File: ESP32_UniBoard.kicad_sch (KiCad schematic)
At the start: 21 parts, among them J1 USB_C_Receptacle_USB2.0, J2 Conn_01x06_Socket, J3 Hirose DF40C, SW1 SW_Push, SW2 SW_Push, U1 ESP32-S3-WROOM-1, U2 SPX3819M5-L-3-3

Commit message: Schematics and PCB updates
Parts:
- added C9: 100nF, Capacitor_SMD:C_0603_1608Metric_Pad1.08x0.95mm_HandSolder, symbol Device:C_Small
- added D3: RED, LED_SMD:LED_0603_1608Metric_Pad1.05x0.95mm_HandSolder, symbol Device:LED
- added D4: YL, LED_SMD:LED_0603_1608Metric_Pad1.05x0.95mm_HandSolder, symbol Device:LED
- added F1: Polyfuse, Fuse:Fuse_1206_3216Metric_Pad1.42x1.75mm_HandSolder, symbol Device:Polyfuse
- added R5, R6: R, Resistor_SMD:R_0603_1608Metric_Pad0.98x0.95mm_HandSolder, symbol Device:R
- added U3: USBLC6-2SC6, Package_TO_SOT_SMD:SOT-23-6, symbol Power_Protection:USBLC6-2SC6
- D2: renamed from D1; value LED -> GRN
- renumbered D2 to D1
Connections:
- net BOOT: now also J3.31 (Pin_31); no longer J3.34 (Pin_34)
- net ESP_RX: now also J3.17 (Pin_17), R5.1; no longer J3.45 (Pin_45)
- net ESP_TX: now also J3.16 (Pin_16); no longer J3.46 (Pin_46)
- net GND: now also C9.2, D3.1 (K), D4.1 (K), U3.2 (GND)
- net GPIO1: now also J3.14 (Pin_14); no longer J3.48 (Pin_48)
- net GPIO10: now also J3.42 (Pin_42); no longer J3.20 (Pin_20)
- net GPIO11: now also J3.41 (Pin_41); no longer J3.21 (Pin_21)
- net GPIO12: now also J3.40 (Pin_40); no longer J3.22 (Pin_22)
- net GPIO13: now also J3.39 (Pin_39); no longer J3.23 (Pin_23)
- net GPIO14: now also J3.37 (Pin_37); no longer J3.28 (Pin_28)
- net GPIO16: now also J3.6 (Pin_6); no longer J3.9 (Pin_9)
- net GPIO17: now also J3.5 (Pin_5); no longer J3.10 (Pin_10)
- net GPIO18: now also J3.4 (Pin_4); no longer J3.11 (Pin_11)
- net GPIO2: now also J3.15 (Pin_15); no longer J3.47 (Pin_47)
- net GPIO21: now also J3.36 (Pin_36); no longer J3.29 (Pin_29)
- net GPIO3: now also J3.46 (Pin_46); no longer J3.16 (Pin_16)
- net GPIO35: now also J3.30 (Pin_30), R6.1; no longer J3.35 (Pin_35)
- net GPIO36: now also J3.29 (Pin_29); no longer J3.36 (Pin_36)
- net GPIO37: now also J3.28 (Pin_28); no longer J3.37 (Pin_37)
- net GPIO38: now also J3.23 (Pin_23); no longer J3.39 (Pin_39)
- net GPIO39: now also J3.22 (Pin_22); no longer J3.40 (Pin_40)
- net GPIO4: now also J3.12 (Pin_12); no longer J3.3 (Pin_3)
- net GPIO40: now also J3.21 (Pin_21); no longer J3.41 (Pin_41)
- net GPIO41: now also J3.20 (Pin_20); no longer J3.42 (Pin_42)
- net GPIO42: now also J3.19 (Pin_19); no longer J3.44 (Pin_44)
- net GPIO46: now also J3.45 (Pin_45); no longer J3.17 (Pin_17)
- net GPIO47: now also J3.35 (Pin_35); no longer J3.30 (Pin_30)
- net GPIO48: now also J3.34 (Pin_34); no longer J3.31 (Pin_31)
- net GPIO5: now also J3.11 (Pin_11); no longer J3.4 (Pin_4)
- net GPIO6: now also J3.10 (Pin_10); no longer J3.5 (Pin_5)
- net GPIO7: now also J3.9 (Pin_9); no longer J3.6 (Pin_6)
- net GPIO8: now also J3.3 (Pin_3); no longer J3.12 (Pin_12)
- net GPIO9: now also J3.44 (Pin_44); no longer J3.19 (Pin_19)
- net USB_D_N: now also J3.47 (Pin_47), U3.1 (I/O1), U3.6 (I/O1); no longer J3.14 (Pin_14)
- net USB_D_P: now also J3.48 (Pin_48), U3.3 (I/O2), U3.4 (I/O2); no longer J3.15 (Pin_15)
- net VBUS: now reaches J1.A4 (VBUS), J1.A9 (VBUS), J1.B4 (VBUS), J1.B9 (VBUS)
- net VBUS: now also C9.1, F1.1, U3.5 (VBUS); no longer D1.2 (A)
- new net: D1.2 (A), F1.2
- new net: D3.2 (A), R5.2
- new net: D4.2 (A), R6.2
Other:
- note added: "GPIO1"
- note added: "PWR"
- note added: "RX"
- moved on the sheet: C2, C5, C6, C7, C8, D1, D2, R4, SW1, SW2, U2

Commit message: Start of PCB routing
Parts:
- added H1, H2, H3, H4: MountingHole, MountingHole:MountingHole_2.7mm_M2.5, symbol Mechanical:MountingHole
- F1: footprint Fuse:Fuse_1206_3216Metric_Pad1.42x1.75mm_HandSolder -> Fuse:Fuse_0805_2012Metric_Pad1.15x1.40mm_HandSolder
- SW1, SW2: footprint Button_Switch_SMD:SW_SPST_PTS645 -> Button_Switch_SMD:SW_Tactile_SPST_NO_Straight_CK_PTS636Sx25SMTRLFS
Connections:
- net GPIO3: now also J3.45 (Pin_45); no longer J3.46 (Pin_46)
- net GPIO46: now also J3.46 (Pin_46); no longer J3.45 (Pin_45)
- net USB_D_N renamed DPr_N
- net DPr_N: no longer J1.A7 (D-), J1.B7 (D-), U3.1 (I/O1)
- net USB_D_P renamed DPr_P
- net DPr_P: no longer J1.A6 (D+), J1.B6 (D+), U3.3 (I/O2)
- new net D_N: J1.A7 (D-), J1.B7 (D-), U3.1 (I/O1)
- new net D_P: J1.A6 (D+), J1.B6 (D+), U3.3 (I/O2)
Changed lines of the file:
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@@
   (no_connect (at 22.86 88.9))
   (no_connect (at 45.72 58.42))
-  (no_connect (at 45.974 81.026))
+  (no_connect (at 45.72 81.28))
   (no_connect (at 45.72 55.88))
   (no_connect (at 45.72 71.12))
-  (no_connect (at 45.974 78.486))
+  (no_connect (at 45.72 78.74))
   (no_connect (at 45.72 66.04))
   (no_connect (at 45.72 48.26))
@@
     (effects (font (size 1.27 1.27)) (justify right bottom))
   )
-  (label "USB_D_N" (at 86.995 132.08 180) (fields_autoplaced)
+  (label "DPr_N" (at 86.995 132.08 180) (fields_autoplaced)
     (effects (font (size 1.27 1.27)) (justify right bottom))
   )
@@
     (effects (font (size 1.27 1.27)) (justify right bottom))
   )
-  (label "USB_D_P" (at 101.6 53.34 180) (fields_autoplaced)
+  (label "DPr_P" (at 101.6 53.34 180) (fields_autoplaced)
     (effects (font (size 1.27 1.27)) (justify right bottom))
   )
@@
     (effects (font (size 1.27 1.27)) (justify left bottom))
   )
-  (label "USB_D_N" (at 62.23 53.34 0) (fields_autoplaced)
+  (label "DPr_N" (at 62.23 53.34 0) (fields_autoplaced)
     (effects (font (size 1.27 1.27)) (justify left bottom))
   )
@@
     (effects (font (size 1.27 1.27)) (justify right bottom))
   )
-  (label "GPIO46" (at 86.995 137.16 180) (fields_autoplaced)
+  (label "GPIO46" (at 86.995 134.62 180) (fields_autoplaced)
     (effects (font (size 1.27 1.27)) (justify right bottom))
   )
@@
     (effects (font (size 1.27 1.27)) (justify right bottom))
   )
-  (label "USB_D_P" (at 86.995 129.54 180) (fields_autoplaced)
+  (label "DPr_P" (at 86.995 129.54 180) (fields_autoplaced)
     (effects (font (size 1.27 1.27)) (justify right bottom))
   )
@@
     (effects (font (size 1.27 1.27)) (justify right bottom))
   )
-  (label "USB_D_N" (at 62.23 58.42 0) (fields_autoplaced)
+  (label "D_N" (at 62.23 58.42 0) (fields_autoplaced)
     (effects (font (size 1.27 1.27)) (justify left bottom))
   )
@@
     (effects (font (size 1.27 1.27)) (justify right bottom))
   )
-  (label "USB_D_N" (at 278.13 41.91 180) (fields_autoplaced)
+  (label "DPr_N" (at 278.13 41.91 180) (fields_autoplaced)
     (effects (font (size 1.27 1.27)) (justify right bottom))
   )
@@
     (effects (font (size 1.27 1.27)) (justify right bottom))
   )
-  (label "USB_D_N" (at 56.642 35.56 180) (fields_autoplaced)
+  (label "D_N" (at 56.642 35.56 180) (fields_autoplaced)
     (effects (font (size 1.27 1.27)) (justify right bottom))
   )
@@
     (effects (font (size 1.27 1.27)) (justify left bottom))
   )
-  (label "GPIO3" (at 86.995 134.62 180) (fields_autoplaced)
+  (label "GPIO3" (at 86.995 137.16 180) (fields_autoplaced)
     (effects (font (size 1.27 1.27)) (justify right bottom))
   )
@@
     (effects (font (size 1.27 1.27)) (justify right bottom))
   )
-  (label "USB_D_P" (at 56.642 40.64 180) (fields_autoplaced)
+  (label "D_P" (at 56.642 40.64 180) (fields_autoplaced)
     (effects (font (size 1.27 1.27)) (justify right bottom))
   )
@@
     (effects (font (size 1.27 1.27)) (justify left bottom))
   )
-  (label "USB_D_P" (at 278.13 39.37 180) (fields_autoplaced)
+  (label "DPr_P" (at 278.13 39.37 180) (fields_autoplaced)
     (effects (font (size 1.27 1.27)) (justify right bottom))
   )
@@
     (effects (font (size 1.27 1.27)) (justify right bottom))
   )
-  (label "USB_D_P" (at 101.6 58.42 180) (fields_autoplaced)
+  (label "D_P" (at 101.6 58.42 180) (fields_autoplaced)
     (effects (font (size 1.27 1.27)) (justify right bottom))
   )
@@
       (effects (font (size 1.27 1.27)) hide)
     )
-    (property "Footprint" "Button_Switch_SMD:SW_SPST_PTS645" (at 260.35 129.54 0)
+    (property "Footprint" "Button_Switch_SMD:SW_Tactile_SPST_NO_Straight_CK_PTS636Sx25SMTRLFS" (at 260.35 129.54 0)
       (effects (font (size 1.27 1.27)) hide)
     )
@@
       (effects (font (size 1.27 1.27)) hide)
     )
-    (property "Footprint" "Button_Switch_SMD:SW_SPST_PTS645" (at 260.35 112.395 0)
+    (property "Footprint" "Button_Switch_SMD:SW_Tactile_SPST_NO_Straight_CK_PTS636Sx25SMTRLFS" (at 260.35 112.395 0)
       (effects (font (size 1.27 1.27)) hide)
     )
@@
         (path "/5887f50f-f688-4449-b0b1-5b01ba454700"
           (reference "#PWR035") (unit 1)
+        )
+      )
+    )
+  )
+  (symbol (lib_id "Mechanical:MountingHole") (at 21.59 178.308 0) (unit 1)
+    (in_bom yes) (on_board yes) (dnp no) (fields_autoplaced)
+    (property "Reference" "H3" (at 24.892 177.673 0)
+      (effects (font (size 1.27 1.27)) (justify left))
+    )
+    (property "Value" "MountingHole" (at 24.892 180.213 0)
+      (effects (font (size 1.27 1.27)) (justify left))
+    )
+    (property "Footprint" "MountingHole:MountingHole_2.7mm_M2.5" (at 21.59 178.308 0)
+      (effects (font (size 1.27 1.27)) hide)
+    )
+    (property "Datasheet" "~" (at 21.59 178.308 0)
+      (effects (font (size 1.27 1.27)) hide)
+    )
+    (instances
+      (project "ESP32_UniBoard"
+        (path "/5887f50f-f688-4449-b0b1-5b01ba454700"
+          (reference "H3") (unit 1)
         )
       )
@@
       (effects (font (size 1.27 1.27)) hide)
     )
-    (property "Footprint" "Fuse:Fuse_1206_3216Metric_Pad1.42x1.75mm_HandSolder" (at 58.42 21.59 0)
+    (property "Footprint" "Fuse:Fuse_0805_2012Metric_Pad1.15x1.40mm_HandSolder" (at 58.42 21.59 0)
       (effects (font (size 1.27 1.27)) (justify left) hide)
     )
@@
         (path "/5887f50f-f688-4449-b0b1-5b01ba454700"
           (reference "#PWR026") (unit 1)
+        )
+      )
+    )
+  )
+  (symbol (lib_id "Mechanical:MountingHole") (at 22.352 191.262 0) (unit 1)
+    (in_bom yes) (on_board yes) (dnp no) (fields_autoplaced)
+    (property "Reference" "H1" (at 25.4 190.627 0)
+      (effects (font (size 1.27 1.27)) (justify left))
+    )
+    (property "Value" "MountingHole" (at 25.4 193.167 0)
+      (effects (font (size 1.27 1.27)) (justify left))
+    )
+    (property "Footprint" "MountingHole:MountingHole_2.7mm_M2.5" (at 22.352 191.262 0)
+      (effects (font (size 1.27 1.27)) hide)
+    )
+    (property "Datasheet" "~" (at 22.352 191.262 0)
+      (effects (font (size 1.27 1.27)) hide)
+    )
+    (instances
+      (project "ESP32_UniBoard"
+        (path "/5887f50f-f688-4449-b0b1-5b01ba454700"
+          (reference "H1") (unit 1)
         )
       )
@@
     )
   )
+  (symbol (lib_id "Mechanical:MountingHole") (at 21.844 170.942 0) (unit 1)
+    (in_bom yes) (on_board yes) (dnp no) (fields_autoplaced)
+    (property "Reference" "H4" (at 25.146 170.307 0)
+      (effects (font (size 1.27 1.27)) (justify left))
+    )
+    (property "Value" "MountingHole" (at 25.146 172.847 0)
+      (effects (font (size 1.27 1.27)) (justify left))
+    )
+    (property "Footprint" "MountingHole:MountingHole_2.7mm_M2.5" (at 21.844 170.942 0)
+      (effects (font (size 1.27 1.27)) hide)
+    )
+    (property "Datasheet" "~" (at 21.844 170.942 0)
+      (effects (font (size 1.27 1.27)) hide)
+    )
+    (instances
+      (project "ESP32_UniBoard"
+        (path "/5887f50f-f688-4449-b0b1-5b01ba454700"
+          (reference "H4") (unit 1)
+        )
+      )
+    )
+  )
   (symbol (lib_id "Device:C_Small") (at 145.415 26.67 0) (unit 1)
     (in_bom yes) (on_board yes) (dnp no)
@@
         )
       )
+    )
+  )
+  (symbol (lib_id "Mechanical:MountingHole") (at 22.098 184.658 0) (unit 1)
+    (in_bom yes) (on_board yes) (dnp no) (fields_autoplaced)
+    (property "Reference" "H2" (at 25.4 184.023 0)
+      (effects (font (size 1.27 1.27)) (justify left))
+    )
+    (property "Value" "MountingHole" (at 25.4 186.563 0)
+      (effects (font (size 1.27 1.27)) (justify left))
+    )
+    (property "Footprint" "MountingHole:MountingHole_2.7mm_M2.5" (at 22.098 184.658 0)
+      (effects (font (size 1.27 1.27)) hide)
+    )
+    (property "Datasheet" "~" (at 22.098 184.658 0)
+      (effects (font (size 1.27 1.27)) hide)
+    )
+    (instances
+      (project "ESP32_UniBoard"
+        (path "/5887f50f-f688-4449-b0b1-5b01ba454700"
+          (reference "H2") (unit 1)
+        )
+      )

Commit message: Routing complete
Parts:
- removed H4: MountingHole, MountingHole:MountingHole_2.7mm_M2.5, symbol Mechanical:MountingHole
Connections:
- net BOOT: now also J3.21 (Pin_21); no longer J3.31 (Pin_31)
- net DPr_N: now also J3.5 (Pin_5); no longer J3.47 (Pin_47)
- net DPr_P: now also J3.4 (Pin_4); no longer J3.48 (Pin_48)
- net ESP_RX: now also J3.35 (Pin_35); no longer J3.17 (Pin_17)
- net ESP_TX: now also J3.36 (Pin_36); no longer J3.16 (Pin_16)
- net GPIO1: now also J3.39 (Pin_39), R6.1; no longer J3.14 (Pin_14)
- net GPIO10: now also J3.10 (Pin_10); no longer J3.42 (Pin_42)
- net GPIO11: now also J3.11 (Pin_11); no longer J3.41 (Pin_41)
- net GPIO12: now also J3.12 (Pin_12); no longer J3.40 (Pin_40)
- net GPIO13: now also J3.14 (Pin_14); no longer J3.39 (Pin_39)
- net GPIO14: now also J3.15 (Pin_15); no longer J3.37 (Pin_37)
- net GPIO15: now also J3.45 (Pin_45); no longer J3.7 (Pin_7)
- net GPIO16: now also J3.46 (Pin_46); no longer J3.6 (Pin_6)
- net GPIO17: now also J3.47 (Pin_47); no longer J3.5 (Pin_5)
- net GPIO18: now also J3.48 (Pin_48); no longer J3.4 (Pin_4)
- net GPIO2: now also J3.37 (Pin_37); no longer J3.15 (Pin_15)
- net GPIO21: now also J3.16 (Pin_16); no longer J3.36 (Pin_36)
- net GPIO3: now also J3.6 (Pin_6); no longer J3.45 (Pin_45)
- net GPIO35: now also J3.22 (Pin_22); no longer J3.30 (Pin_30), R6.1
- net GPIO36: now also J3.23 (Pin_23); no longer J3.29 (Pin_29)
- net GPIO38: now also J3.29 (Pin_29); no longer J3.23 (Pin_23)
- net GPIO39: now also J3.30 (Pin_30); no longer J3.22 (Pin_22)
- net GPIO4: now also J3.40 (Pin_40); no longer J3.12 (Pin_12)
- net GPIO40: now also J3.31 (Pin_31); no longer J3.21 (Pin_21)
- net GPIO41: now also J3.32 (Pin_32); no longer J3.20 (Pin_20)
- net GPIO42: now also J3.34 (Pin_34); no longer J3.19 (Pin_19)
- net GPIO45: now also J3.20 (Pin_20); no longer J3.32 (Pin_32)
- net GPIO46: now also J3.7 (Pin_7); no longer J3.46 (Pin_46)
- net GPIO47: now also J3.17 (Pin_17); no longer J3.35 (Pin_35)
- net GPIO48: now also J3.19 (Pin_19); no longer J3.34 (Pin_34)
- net GPIO5: now also J3.41 (Pin_41); no longer J3.11 (Pin_11)
- net GPIO6: now also J3.42 (Pin_42); no longer J3.10 (Pin_10)
- net GPIO7: now also J3.44 (Pin_44); no longer J3.9 (Pin_9)
- net GPIO9: now also J3.9 (Pin_9); no longer J3.44 (Pin_44)

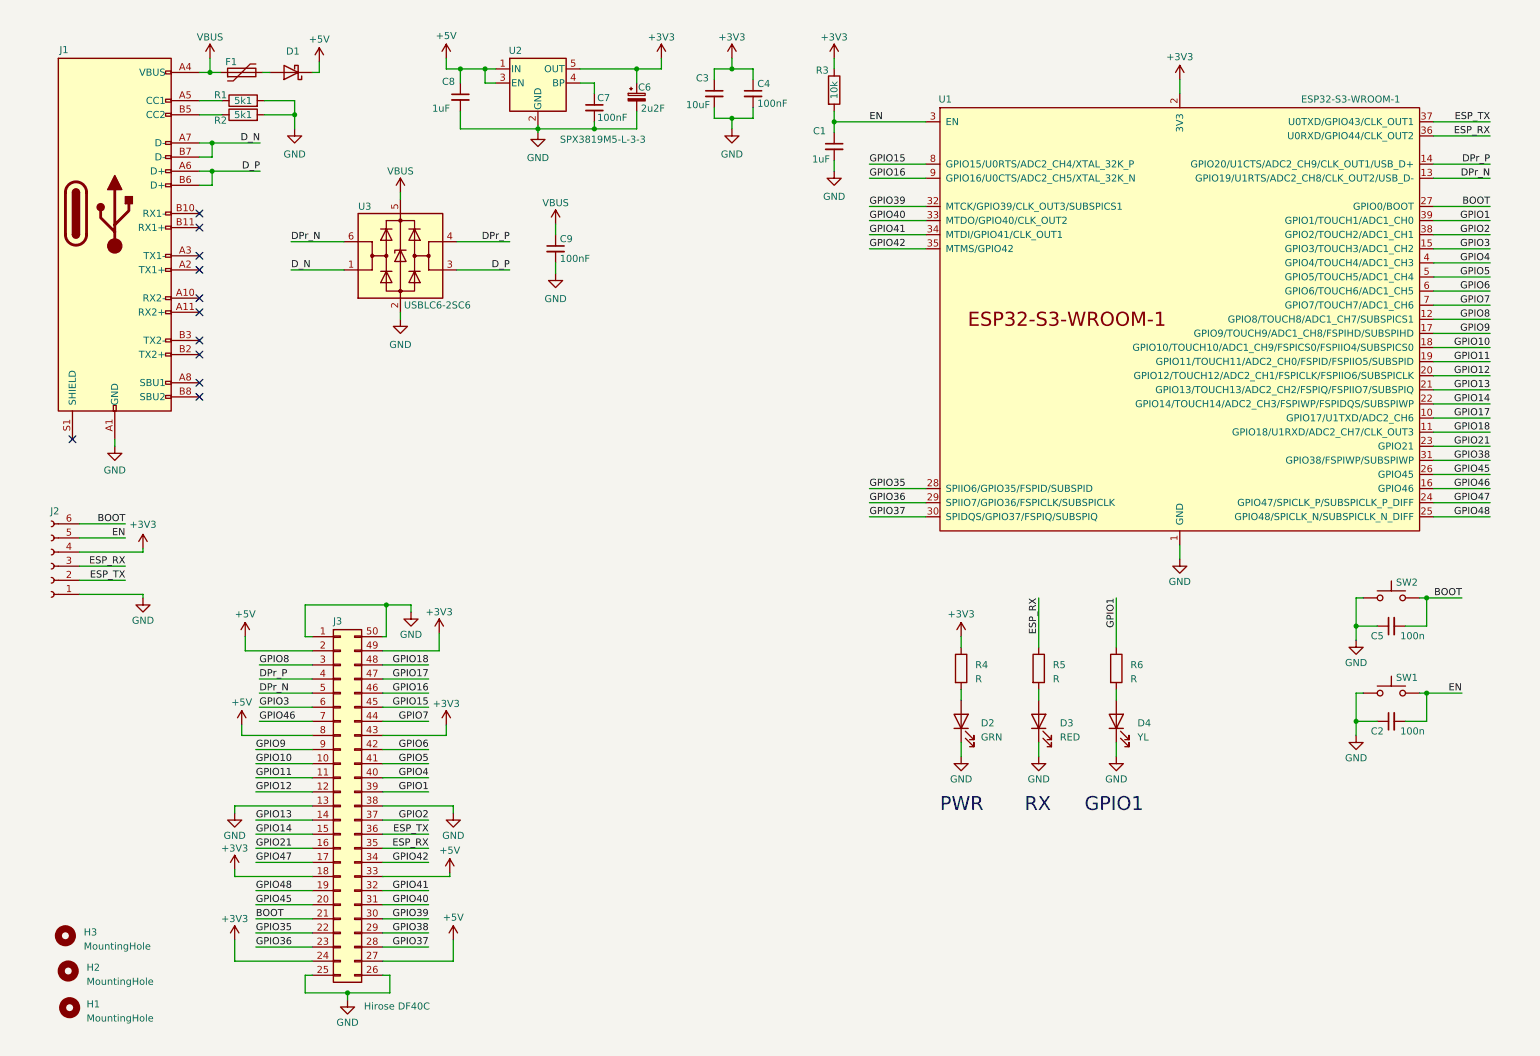
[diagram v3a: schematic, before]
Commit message: Screenshots generated
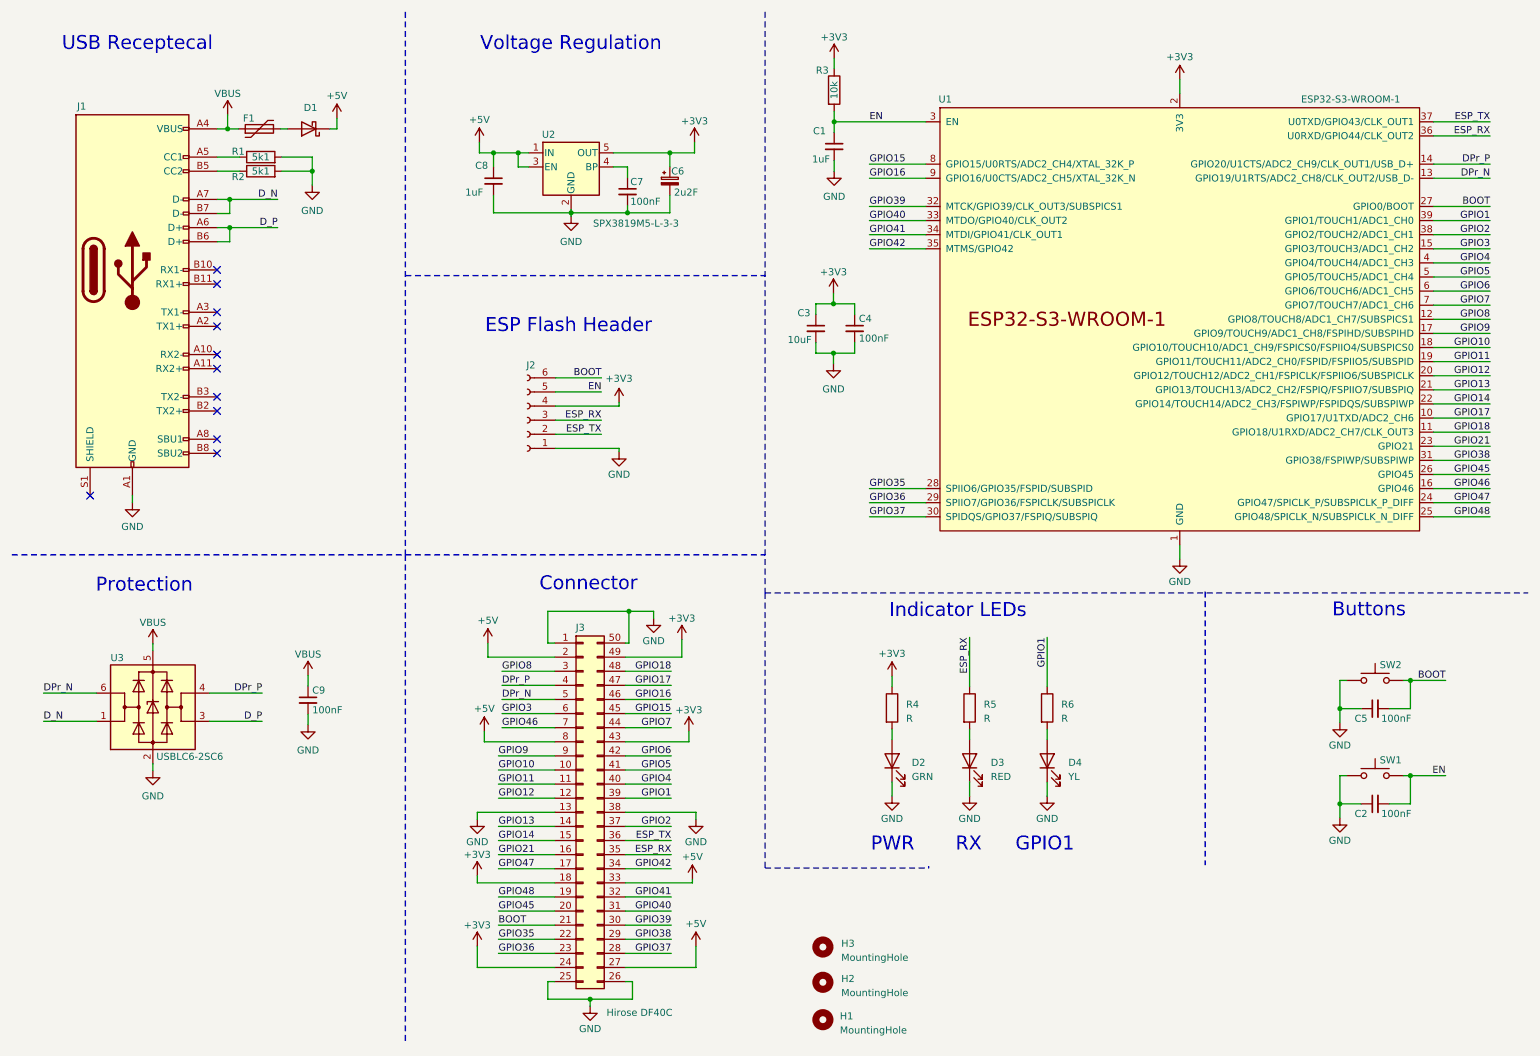
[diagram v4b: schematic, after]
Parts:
- C2, C5: value 100n -> 100nF
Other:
- note added: "Buttons"
- note added: "Connector"
- note added: "ESP Flash Header"
- note added: "Indicator LEDs"
- note added: "Protection"
- note added: "USB Receptecal"
- note added: "Voltage Regulation"
- moved on the sheet: C2, C3, C4, C5, C6, C7, C8, C9, D1, D2, D3, D4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

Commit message: Adjustments in Schematic and PCB
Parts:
- J2: symbol Connector:Conn_01x06_Socket -> Connector_Generic:Conn_01x06
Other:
- moved on the sheet: C6, C7, C8, C9, U2, U3

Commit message: -
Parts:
- J3: footprint Hirose_Connector_DF40C:Hirose_DF40C-50 -> Hirose_Connector_DF40C:Hirose_DF40C-50DS
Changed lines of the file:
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@@
       (effects (font (size 1.27 1.27)))
     )
-    (property "Footprint" "Hirose_Connector_DF40C:Hirose_DF40C-50" (at 114.808 156.083 0)
+    (property "Footprint" "Hirose_Connector_DF40C:Hirose_DF40C-50DS" (at 114.808 156.083 0)
       (effects (font (size 1.27 1.27)) hide)
     )
